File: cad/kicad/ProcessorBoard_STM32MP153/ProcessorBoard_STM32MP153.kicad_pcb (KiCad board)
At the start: 6 copper layers, 50 x 50 mm, 87 parts, among them IC301 STPMIC1BPQR, IC401 IS43LD16320A-25BLI, J201 Conn_01x03_Pin, J301 Conn_01x01_Pin, J501 SFP, U201 STM32MP153CACx, X201 ECS-3225MVQ-240-CN-TR, X501 RTL8211FS(I)-xx-xx

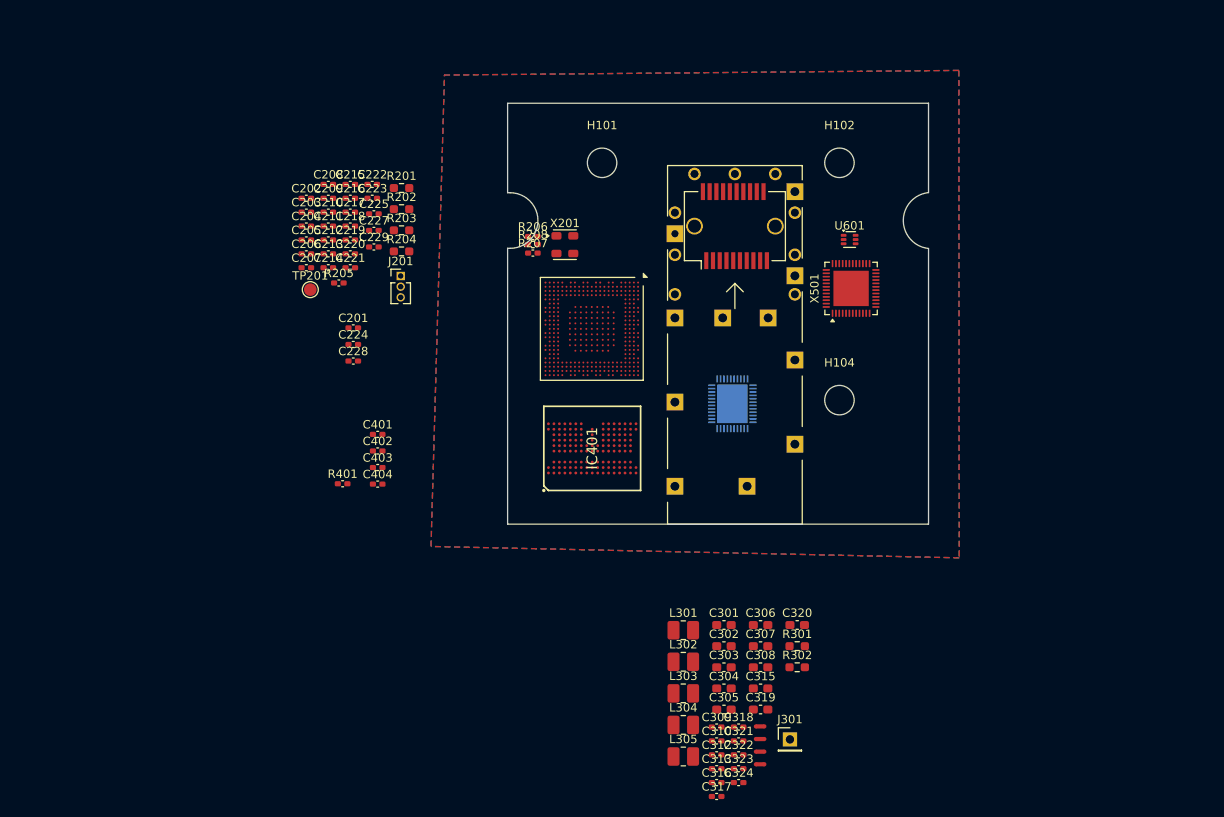
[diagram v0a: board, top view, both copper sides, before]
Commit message: new ram
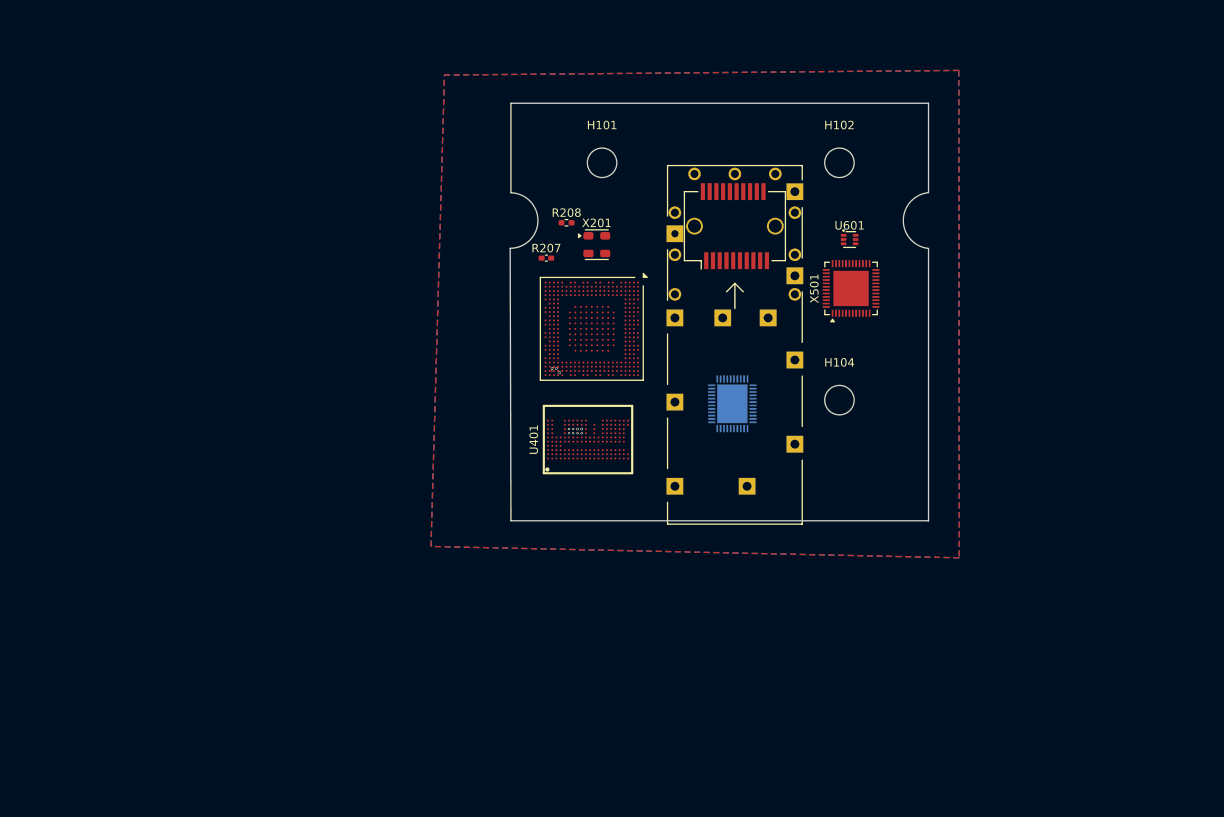
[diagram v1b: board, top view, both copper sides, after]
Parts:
- removed C201, C224, C225, C227, C228, C229, C401, C402, C403, C404: 100n, Capacitor_SMD:C_0402_1005Metric_Pad0.74x0.62mm_HandSolder
- removed C202, C203, C204, C205, C206, C207, C208, C209, C210, C211, C212, C213, C214, C215, C216, C217, C218, C221, C222, C223, C309, C312, C316, C317, C321, C324: 1u, Capacitor_SMD:C_0402_1005Metric_Pad0.74x0.62mm_HandSolder
- removed C219, C220: 1n, Capacitor_SMD:C_0402_1005Metric_Pad0.74x0.62mm_HandSolder
- removed C301, C303, C305, C307, C315, C319, C320: 10u, Capacitor_SMD:C_0603_1608Metric_Pad1.08x0.95mm_HandSolder
- removed C302, C304, C306, C308: 22u, Capacitor_SMD:C_0603_1608Metric_Pad1.08x0.95mm_HandSolder
- removed C310, C313, C318, C322, C323: 4.7u, Capacitor_SMD:C_0402_1005Metric_Pad0.74x0.62mm_HandSolder
- removed IC401: IS43LD16320A-25BLI, __WM_Local:BGA134C65P10X17_1000X1150X110
- removed J201: Conn_01x03_Pin, Connector_PinHeader_1.27mm:PinHeader_1x03_P1.27mm_Vertical
- removed J301: Conn_01x01_Pin, Connector_PinHeader_2.54mm:PinHeader_1x01_P2.54mm_Vertical
- removed L301, L302, L303, L304, L305: 1u, Inductor_SMD:L_1008_2520Metric_Pad1.43x2.20mm_HandSolder
- removed NT301, NT302, NT303, NT304: NetTie_2, NetTie:NetTie-2_SMD_Pad0.5mm
- removed R201, R202, R204: 47k, Resistor_SMD:R_0603_1608Metric_Pad0.98x0.95mm_HandSolder
- removed R203: 3090, Resistor_SMD:R_0603_1608Metric_Pad0.98x0.95mm_HandSolder
- removed R205, R401: 240, Capacitor_SMD:C_0402_1005Metric_Pad0.74x0.62mm_HandSolder
- removed R206: 10k, Capacitor_SMD:C_0402_1005Metric_Pad0.74x0.62mm_HandSolder
- removed R301, R302: 1.2k, Resistor_SMD:R_0603_1608Metric_Pad0.98x0.95mm_HandSolder
- removed TP201: TestPoint, TestPoint:TestPoint_Pad_D1.5mm
- added U401: XT61M2G8D2TA-B8BEA, __WM_Local:FBGA-162_L10.5-W8.0-P0.50_XT61M4G8D2TA, F.Cu at (139.6, 110.0)
- moved R208 4.76 mm to (137.0, 84.2)
- moved X201 3.80 mm to (140.6, 86.8)
- moved R207 1.71 mm to (134.6, 88.4)
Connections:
- J501 pad 1: Net-(J501-VeeT-Pad1) -> GND
- J501 pad 10: Net-(J501-VeeR-Pad10) -> GND
- J501 pad 11: Net-(J501-VeeR-Pad10) -> GND
- J501 pad 12: unconnected-(J501-RD--Pad12) -> /SPF/RD-
- J501 pad 13: unconnected-(J501-RD+-Pad13) -> /SPF/RD+
- J501 pad 14: Net-(J501-VeeR-Pad10) -> GND
- J501 pad 15: unconnected-(J501-VccR-Pad15) -> /SPF/3v3 3A_{max}
- J501 pad 16: unconnected-(J501-VccT-Pad16) -> /SPF/3v3 3A_{max}
- J501 pad 17: Net-(J501-VeeT-Pad1) -> GND
- J501 pad 18: unconnected-(J501-TD+-Pad18) -> /SPF/TD+
- J501 pad 19: unconnected-(J501-TD--Pad19) -> /SPF/TD-
- J501 pad 20: Net-(J501-VeeT-Pad1) -> GND
- J501 pad 4: unconnected-(J501-MOD_DEF2-Pad4) -> /SPF/MOD_SDA
- J501 pad 5: unconnected-(J501-MOD_DEF1-Pad5) -> /SPF/MOD_SCL
- J501 pad 6: unconnected-(J501-MOD_DEF0-Pad6) -> /SPF/MOD_PRZ
- J501 pad 9: Net-(J501-VeeR-Pad10) -> GND
- U601 pad 1: unconnected-(U601-GND-Pad1) -> GND
- U601 pad 2: unconnected-(U601-SW-Pad2) -> Net-(U601-SW)
- U601 pad 3: unconnected-(U601-V_{in}-Pad3) -> /Power SPF/OB_5v
- U601 pad 4: unconnected-(U601-EN-Pad4) -> /Power SPF/enable
- U601 pad 5: unconnected-(U601-FB-Pad5) -> Net-(U601-FB)
- X501 pad 1: unconnected-(X501-AV_{dd}3v3-Pad1) -> /SPF/3v3 3A_{max}
- X501 pad 12: unconnected-(X501-AV_{dd}3v3-Pad12) -> /SPF/3v3 3A_{max}
- X501 pad 22: unconnected-(X501-DV_{dd}1v0-Pad22) -> Net-(C502-Pad1)
- X501 pad 30: unconnected-(X501-AV_{dd}3v3-Pad30) -> /SPF/3v3 3A_{max}
- X501 pad 31: unconnected-(X501-V_{dd}_REG-Pad31) -> /SPF/3v3 3A_{max}
- X501 pad 32: unconnected-(X501-REG_OUT-Pad32) -> Net-(X501-REG_OUT)
- X501 pad 4: unconnected-(X501-AV_{dd}1v0-Pad4) -> Net-(C502-Pad1)
- X501 pad 45: unconnected-(X501-XTAL_IN-Pad45) -> /SPF/xtal_in
- X501 pad 46: unconnected-(X501-XTAL_OUT-Pad46) -> /SPF/xtal_out
- X501 pad 47: unconnected-(X501-DV_{dd}1v0-Pad47) -> Net-(C502-Pad1)
- X501 pad 48: unconnected-(X501-RSET-Pad48) -> /SPF/reset
- X501 pad 49: unconnected-(X501-GND-Pad49) -> GND
- X501 pad 9: unconnected-(X501-AV_{dd}1v0-Pad9) -> Net-(C502-Pad1)
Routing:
- net unconnected-(U401-DM3-PadH7): track 0.00 -> 0.95 mm, vias 0 -> 1
- net GND: track 0.00 -> 0.70 mm, vias 0 -> 1
- net /d15: track 0.00 -> 0.31 mm, vias 0 -> 2
- net unconnected-(U201-DDR_DQ25-PadY22): track 0.00 -> 0.28 mm, vias 0 -> 1
- net /d14: track 0.00 -> 0.10 mm, vias 0 -> 1
- net unconnected-(U401-DQS3-PadG8): vias 0 -> 1
- net unconnected-(U401-DQ27-PadG7): vias 0 -> 1
- net unconnected-(U401-DQ25-PadF8): vias 0 -> 1
- net /d13: vias 0 -> 1
- net /V_{dd_DDRQ}: vias 0 -> 1
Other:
- board size 50 x 50 mm -> 49.7 x 49.6 mm

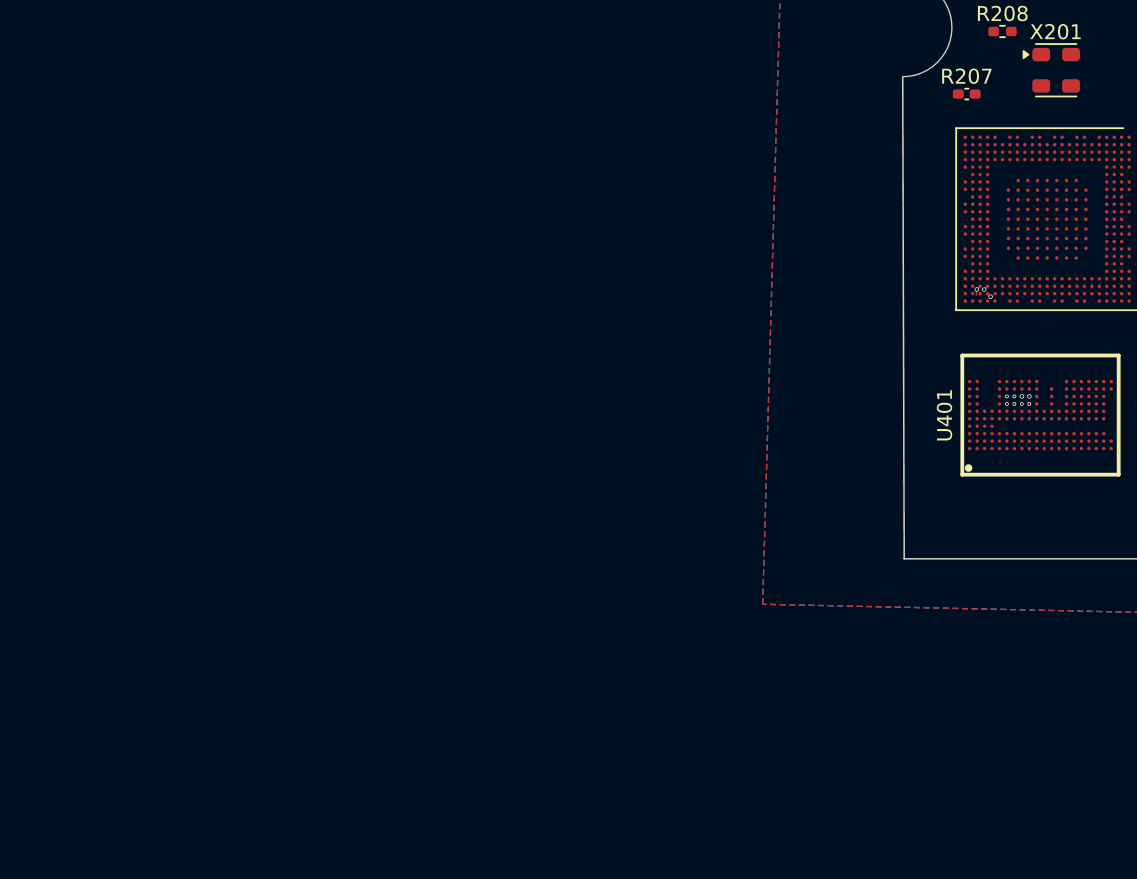
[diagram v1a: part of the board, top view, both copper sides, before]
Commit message: realtek bridge thing somewhat more wired
apparently the proper term for via skimping and what not is NFPR (non functional pad removal). all my homies love NFPR. so it is possible to route 0.5mm bga. still fighting the dog but at least cant bring it to another layer
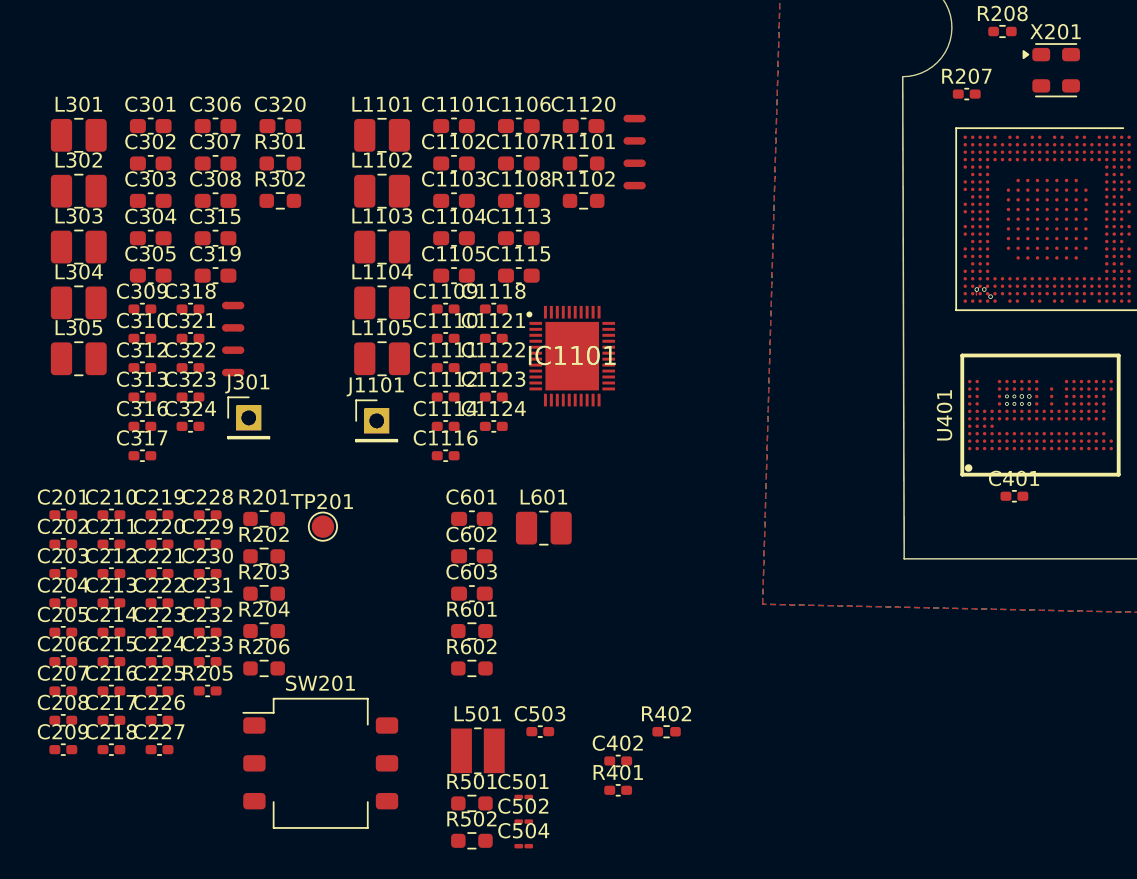
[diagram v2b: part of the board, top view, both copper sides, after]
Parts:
- added C1101: 10u, Capacitor_SMD:C_0603_1608Metric_Pad1.08x0.95mm_HandSolder, F.Cu at (100.2, 90.5)
- added C1102: 10u, Capacitor_SMD:C_0603_1608Metric_Pad1.08x0.95mm_HandSolder, F.Cu at (100.2, 93.1)
- added C1103: 10u, Capacitor_SMD:C_0603_1608Metric_Pad1.08x0.95mm_HandSolder, F.Cu at (100.2, 95.6)
- added C1104: 10u, Capacitor_SMD:C_0603_1608Metric_Pad1.08x0.95mm_HandSolder, F.Cu at (100.2, 98.1)
- added C1105: 22u, Capacitor_SMD:C_0603_1608Metric_Pad1.08x0.95mm_HandSolder, F.Cu at (100.2, 100.6)
- added C1106: 22u, Capacitor_SMD:C_0603_1608Metric_Pad1.08x0.95mm_HandSolder, F.Cu at (104.5, 90.5)
- added C1107: 22u, Capacitor_SMD:C_0603_1608Metric_Pad1.08x0.95mm_HandSolder, F.Cu at (104.5, 93.1)
- added C1108: 22u, Capacitor_SMD:C_0603_1608Metric_Pad1.08x0.95mm_HandSolder, F.Cu at (104.5, 95.6)
- added C1109: 4.7u, Capacitor_SMD:C_0402_1005Metric_Pad0.74x0.62mm_HandSolder, F.Cu at (99.6, 102.8)
- added C1110: 4.7u, Capacitor_SMD:C_0402_1005Metric_Pad0.74x0.62mm_HandSolder, F.Cu at (99.6, 104.8)
- added C1111: 1u, Capacitor_SMD:C_0402_1005Metric_Pad0.74x0.62mm_HandSolder, F.Cu at (99.6, 106.8)
- added C1112: 1u, Capacitor_SMD:C_0402_1005Metric_Pad0.74x0.62mm_HandSolder, F.Cu at (99.6, 108.7)
- added C1113: 10u, Capacitor_SMD:C_0603_1608Metric_Pad1.08x0.95mm_HandSolder, F.Cu at (104.5, 98.1)
- added C1114: 1u, Capacitor_SMD:C_0402_1005Metric_Pad0.74x0.62mm_HandSolder, F.Cu at (99.6, 110.7)
- added C1115: 10u, Capacitor_SMD:C_0603_1608Metric_Pad1.08x0.95mm_HandSolder, F.Cu at (104.5, 100.6)
- added C1116: 4.7u, Capacitor_SMD:C_0402_1005Metric_Pad0.74x0.62mm_HandSolder, F.Cu at (99.6, 112.7)
- added C1118: 4.7u, Capacitor_SMD:C_0402_1005Metric_Pad0.74x0.62mm_HandSolder, F.Cu at (102.8, 102.8)
- added C1120: 10u, Capacitor_SMD:C_0603_1608Metric_Pad1.08x0.95mm_HandSolder, F.Cu at (108.9, 90.5)
- added C1121: 1u, Capacitor_SMD:C_0402_1005Metric_Pad0.74x0.62mm_HandSolder, F.Cu at (102.8, 104.8)
- added C1122: 4.7u, Capacitor_SMD:C_0402_1005Metric_Pad0.74x0.62mm_HandSolder, F.Cu at (102.8, 106.8)
- added C1123: 1u, Capacitor_SMD:C_0402_1005Metric_Pad0.74x0.62mm_HandSolder, F.Cu at (102.8, 108.7)
- added C1124: 1u, Capacitor_SMD:C_0402_1005Metric_Pad0.74x0.62mm_HandSolder, F.Cu at (102.8, 110.7)
- added C201: 100n, Capacitor_SMD:C_0402_1005Metric_Pad0.74x0.62mm_HandSolder, F.Cu at (74.0, 116.7)
- added C202: 1u, Capacitor_SMD:C_0402_1005Metric_Pad0.74x0.62mm_HandSolder, F.Cu at (74.0, 118.6)
- added C203: 1u, Capacitor_SMD:C_0402_1005Metric_Pad0.74x0.62mm_HandSolder, F.Cu at (74.0, 120.6)
- added C204: 1u, Capacitor_SMD:C_0402_1005Metric_Pad0.74x0.62mm_HandSolder, F.Cu at (74.0, 122.6)
- added C205: 1u, Capacitor_SMD:C_0402_1005Metric_Pad0.74x0.62mm_HandSolder, F.Cu at (74.0, 124.5)
- added C206: 1u, Capacitor_SMD:C_0402_1005Metric_Pad0.74x0.62mm_HandSolder, F.Cu at (74.0, 126.5)
- added C207: 1u, Capacitor_SMD:C_0402_1005Metric_Pad0.74x0.62mm_HandSolder, F.Cu at (74.0, 128.5)
- added C208: 1u, Capacitor_SMD:C_0402_1005Metric_Pad0.74x0.62mm_HandSolder, F.Cu at (74.0, 130.4)
- added C209: 1u, Capacitor_SMD:C_0402_1005Metric_Pad0.74x0.62mm_HandSolder, F.Cu at (74.0, 132.4)
- added C210: 1u, Capacitor_SMD:C_0402_1005Metric_Pad0.74x0.62mm_HandSolder, F.Cu at (77.2, 116.7)
- added C211: 1u, Capacitor_SMD:C_0402_1005Metric_Pad0.74x0.62mm_HandSolder, F.Cu at (77.2, 118.6)
- added C212: 1u, Capacitor_SMD:C_0402_1005Metric_Pad0.74x0.62mm_HandSolder, F.Cu at (77.2, 120.6)
- added C213: 1u, Capacitor_SMD:C_0402_1005Metric_Pad0.74x0.62mm_HandSolder, F.Cu at (77.2, 122.6)
- added C214: 1u, Capacitor_SMD:C_0402_1005Metric_Pad0.74x0.62mm_HandSolder, F.Cu at (77.2, 124.5)
- added C215: 1u, Capacitor_SMD:C_0402_1005Metric_Pad0.74x0.62mm_HandSolder, F.Cu at (77.2, 126.5)
- added C216: 1u, Capacitor_SMD:C_0402_1005Metric_Pad0.74x0.62mm_HandSolder, F.Cu at (77.2, 128.5)
- added C217: 1u, Capacitor_SMD:C_0402_1005Metric_Pad0.74x0.62mm_HandSolder, F.Cu at (77.2, 130.4)
- added C218: 1u, Capacitor_SMD:C_0402_1005Metric_Pad0.74x0.62mm_HandSolder, F.Cu at (77.2, 132.4)
- added C219: 1n, Capacitor_SMD:C_0402_1005Metric_Pad0.74x0.62mm_HandSolder, F.Cu at (80.4, 116.7)
- added C220: 1n, Capacitor_SMD:C_0402_1005Metric_Pad0.74x0.62mm_HandSolder, F.Cu at (80.4, 118.6)
- added C221: 1u, Capacitor_SMD:C_0402_1005Metric_Pad0.74x0.62mm_HandSolder, F.Cu at (80.4, 120.6)
- added C222: 1u, Capacitor_SMD:C_0402_1005Metric_Pad0.74x0.62mm_HandSolder, F.Cu at (80.4, 122.6)
- added C223: 1u, Capacitor_SMD:C_0402_1005Metric_Pad0.74x0.62mm_HandSolder, F.Cu at (80.4, 124.5)
- added C224: 100n, Capacitor_SMD:C_0402_1005Metric_Pad0.74x0.62mm_HandSolder, F.Cu at (80.4, 126.5)
- added C225: 100n, Capacitor_SMD:C_0402_1005Metric_Pad0.74x0.62mm_HandSolder, F.Cu at (80.4, 128.5)
- added C226: 1u, Capacitor_SMD:C_0402_1005Metric_Pad0.74x0.62mm_HandSolder, F.Cu at (80.4, 130.4)
- added C227: 100n, Capacitor_SMD:C_0402_1005Metric_Pad0.74x0.62mm_HandSolder, F.Cu at (80.4, 132.4)
- added C228: 100n, Capacitor_SMD:C_0402_1005Metric_Pad0.74x0.62mm_HandSolder, F.Cu at (83.6, 116.7)
- added C229: 100n, Capacitor_SMD:C_0402_1005Metric_Pad0.74x0.62mm_HandSolder, F.Cu at (83.6, 118.6)
- added C230: 1u, Capacitor_SMD:C_0402_1005Metric_Pad0.74x0.62mm_HandSolder, F.Cu at (83.6, 120.6)
- added C231: 1u, Capacitor_SMD:C_0402_1005Metric_Pad0.74x0.62mm_HandSolder, F.Cu at (83.6, 122.6)
- added C232: 1u, Capacitor_SMD:C_0402_1005Metric_Pad0.74x0.62mm_HandSolder, F.Cu at (83.6, 124.5)
- added C233: 1u, Capacitor_SMD:C_0402_1005Metric_Pad0.74x0.62mm_HandSolder, F.Cu at (83.6, 126.5)
- added C301: 10u, Capacitor_SMD:C_0603_1608Metric_Pad1.08x0.95mm_HandSolder, F.Cu at (79.8, 90.5)
- added C302: 22u, Capacitor_SMD:C_0603_1608Metric_Pad1.08x0.95mm_HandSolder, F.Cu at (79.8, 93.1)
- added C303: 10u, Capacitor_SMD:C_0603_1608Metric_Pad1.08x0.95mm_HandSolder, F.Cu at (79.8, 95.6)
- added C304: 22u, Capacitor_SMD:C_0603_1608Metric_Pad1.08x0.95mm_HandSolder, F.Cu at (79.8, 98.1)
- added C305: 10u, Capacitor_SMD:C_0603_1608Metric_Pad1.08x0.95mm_HandSolder, F.Cu at (79.8, 100.6)
- added C306: 22u, Capacitor_SMD:C_0603_1608Metric_Pad1.08x0.95mm_HandSolder, F.Cu at (84.2, 90.5)
- added C307: 10u, Capacitor_SMD:C_0603_1608Metric_Pad1.08x0.95mm_HandSolder, F.Cu at (84.2, 93.1)
- added C308: 22u, Capacitor_SMD:C_0603_1608Metric_Pad1.08x0.95mm_HandSolder, F.Cu at (84.2, 95.6)
- added C309: 1u, Capacitor_SMD:C_0402_1005Metric_Pad0.74x0.62mm_HandSolder, F.Cu at (79.3, 102.8)
- added C310: 4.7u, Capacitor_SMD:C_0402_1005Metric_Pad0.74x0.62mm_HandSolder, F.Cu at (79.3, 104.8)
- added C312: 1u, Capacitor_SMD:C_0402_1005Metric_Pad0.74x0.62mm_HandSolder, F.Cu at (79.3, 106.8)
- added C313: 4.7u, Capacitor_SMD:C_0402_1005Metric_Pad0.74x0.62mm_HandSolder, F.Cu at (79.3, 108.7)
- added C315: 10u, Capacitor_SMD:C_0603_1608Metric_Pad1.08x0.95mm_HandSolder, F.Cu at (84.2, 98.1)
- added C316: 1u, Capacitor_SMD:C_0402_1005Metric_Pad0.74x0.62mm_HandSolder, F.Cu at (79.3, 110.7)
- added C317: 1u, Capacitor_SMD:C_0402_1005Metric_Pad0.74x0.62mm_HandSolder, F.Cu at (79.3, 112.7)
- added C318: 4.7u, Capacitor_SMD:C_0402_1005Metric_Pad0.74x0.62mm_HandSolder, F.Cu at (82.5, 102.8)
- added C319: 10u, Capacitor_SMD:C_0603_1608Metric_Pad1.08x0.95mm_HandSolder, F.Cu at (84.2, 100.6)
- added C320: 10u, Capacitor_SMD:C_0603_1608Metric_Pad1.08x0.95mm_HandSolder, F.Cu at (88.5, 90.5)
- added C321: 1u, Capacitor_SMD:C_0402_1005Metric_Pad0.74x0.62mm_HandSolder, F.Cu at (82.5, 104.8)
- added C322: 4.7u, Capacitor_SMD:C_0402_1005Metric_Pad0.74x0.62mm_HandSolder, F.Cu at (82.5, 106.8)
- added C323: 4.7u, Capacitor_SMD:C_0402_1005Metric_Pad0.74x0.62mm_HandSolder, F.Cu at (82.5, 108.7)
- added C324: 1u, Capacitor_SMD:C_0402_1005Metric_Pad0.74x0.62mm_HandSolder, F.Cu at (82.5, 110.7)
- added C401: 100n, Capacitor_SMD:C_0402_1005Metric_Pad0.74x0.62mm_HandSolder, F.Cu at (137.8, 115.4)
- added C402: 100n, Capacitor_SMD:C_0402_1005Metric_Pad0.74x0.62mm_HandSolder, F.Cu at (111.2, 133.2)
- added C501: 4.7u, Capacitor_SMD:C_01005_0402Metric_Pad0.57x0.30mm_HandSolder, F.Cu at (104.9, 135.6)
- added C502: 4.7u, Capacitor_SMD:C_01005_0402Metric_Pad0.57x0.30mm_HandSolder, F.Cu at (104.9, 137.2)
- added C503: 100n, Capacitor_SMD:C_0402_1005Metric_Pad0.74x0.62mm_HandSolder, F.Cu at (106.0, 131.2)
- added C504: 4.7u, Capacitor_SMD:C_01005_0402Metric_Pad0.57x0.30mm_HandSolder, F.Cu at (104.9, 138.9)
- added C601: 10u, Capacitor_SMD:C_0603_1608Metric_Pad1.08x0.95mm_HandSolder, F.Cu at (101.4, 116.9)
- added C602: 10u, Capacitor_SMD:C_0603_1608Metric_Pad1.08x0.95mm_HandSolder, F.Cu at (101.4, 119.4)
- added C603: 10u, Capacitor_SMD:C_0603_1608Metric_Pad1.08x0.95mm_HandSolder, F.Cu at (101.4, 121.9)
- added IC1101: STPMIC1BPQR, __WM_Local:QFN40P500X600X80-45N-D, F.Cu at (108.1, 106.0)
- added J1101: Conn_01x01_Pin, Connector_PinHeader_2.54mm:PinHeader_1x01_P2.54mm_Vertical, F.Cu at (95.0, 110.3)
- added J301: Conn_01x01_Pin, Connector_PinHeader_2.54mm:PinHeader_1x01_P2.54mm_Vertical, F.Cu at (86.4, 110.1)
- added L1101: 1u, Inductor_SMD:L_1008_2520Metric_Pad1.43x2.20mm_HandSolder, F.Cu at (95.3, 91.2)
- added L1102: 1u, Inductor_SMD:L_1008_2520Metric_Pad1.43x2.20mm_HandSolder, F.Cu at (95.3, 94.9)
- added L1103: 1u, Inductor_SMD:L_1008_2520Metric_Pad1.43x2.20mm_HandSolder, F.Cu at (95.3, 98.7)
- added L1104: 1u, Inductor_SMD:L_1008_2520Metric_Pad1.43x2.20mm_HandSolder, F.Cu at (95.3, 102.4)
- added L1105: 1u, Inductor_SMD:L_1008_2520Metric_Pad1.43x2.20mm_HandSolder, F.Cu at (95.3, 106.2)
- added L301: 1u, Inductor_SMD:L_1008_2520Metric_Pad1.43x2.20mm_HandSolder, F.Cu at (75.0, 91.2)
- added L302: 1u, Inductor_SMD:L_1008_2520Metric_Pad1.43x2.20mm_HandSolder, F.Cu at (75.0, 94.9)
- added L303: 1u, Inductor_SMD:L_1008_2520Metric_Pad1.43x2.20mm_HandSolder, F.Cu at (75.0, 98.7)
- added L304: 1u, Inductor_SMD:L_1008_2520Metric_Pad1.43x2.20mm_HandSolder, F.Cu at (75.0, 102.4)
- added L305: 1u, Inductor_SMD:L_1008_2520Metric_Pad1.43x2.20mm_HandSolder, F.Cu at (75.0, 106.2)
- added L501: 2.2u, Inductor_SMD:L_Ferrocore_DLG-0302, F.Cu at (101.8, 132.5)
- added L601: 1u, Inductor_SMD:L_1008_2520Metric_Pad1.43x2.20mm_HandSolder, F.Cu at (106.2, 117.5)
- added NT1101: NetTie_2, NetTie:NetTie-2_SMD_Pad0.5mm, F.Cu at (112.3, 90.0)
- added NT1102: NetTie_2, NetTie:NetTie-2_SMD_Pad0.5mm, F.Cu at (112.3, 91.5)
- added NT1103: NetTie_2, NetTie:NetTie-2_SMD_Pad0.5mm, F.Cu at (112.3, 93.0)
- added NT1104: NetTie_2, NetTie:NetTie-2_SMD_Pad0.5mm, F.Cu at (112.3, 94.5)
- added NT301: NetTie_2, NetTie:NetTie-2_SMD_Pad0.5mm, F.Cu at (85.4, 102.6)
- added NT302: NetTie_2, NetTie:NetTie-2_SMD_Pad0.5mm, F.Cu at (85.4, 104.1)
- added NT303: NetTie_2, NetTie:NetTie-2_SMD_Pad0.5mm, F.Cu at (85.4, 105.6)
- added NT304: NetTie_2, NetTie:NetTie-2_SMD_Pad0.5mm, F.Cu at (85.4, 107.1)
- added R1101: 1.2k, Resistor_SMD:R_0603_1608Metric_Pad0.98x0.95mm_HandSolder, F.Cu at (108.9, 93.1)
- added R1102: 1.2k, Resistor_SMD:R_0603_1608Metric_Pad0.98x0.95mm_HandSolder, F.Cu at (108.9, 95.6)
- added R201: 45.3k, Resistor_SMD:R_0603_1608Metric_Pad0.98x0.95mm_HandSolder, F.Cu at (87.4, 116.9)
- added R202: 45.3k, Resistor_SMD:R_0603_1608Metric_Pad0.98x0.95mm_HandSolder, F.Cu at (87.4, 119.4)
- added R203: 45.3k, Resistor_SMD:R_0603_1608Metric_Pad0.98x0.95mm_HandSolder, F.Cu at (87.4, 121.9)
- added R204: 1.2k, Resistor_SMD:R_0603_1608Metric_Pad0.98x0.95mm_HandSolder, F.Cu at (87.4, 124.5)
- added R205: 240, Capacitor_SMD:C_0402_1005Metric_Pad0.74x0.62mm_HandSolder, F.Cu at (83.6, 128.5)
- added R206: 10k, Resistor_SMD:R_0603_1608Metric_Pad0.98x0.95mm_HandSolder, F.Cu at (87.4, 127.0)
- added R301: 1.2k, Resistor_SMD:R_0603_1608Metric_Pad0.98x0.95mm_HandSolder, F.Cu at (88.5, 93.1)
- added R302: 1.2k, Resistor_SMD:R_0603_1608Metric_Pad0.98x0.95mm_HandSolder, F.Cu at (88.5, 95.6)
- added R401: 240, Capacitor_SMD:C_0402_1005Metric_Pad0.74x0.62mm_HandSolder, F.Cu at (111.2, 135.1)
- added R402: 100, Resistor_SMD:R_0402_1005Metric_Pad0.72x0.64mm_HandSolder, F.Cu at (114.5, 131.2)
- added R501: 1.2k, Resistor_SMD:R_0603_1608Metric_Pad0.98x0.95mm_HandSolder, F.Cu at (101.4, 136.0)
- added R502: 1.2k, Resistor_SMD:R_0603_1608Metric_Pad0.98x0.95mm_HandSolder, F.Cu at (101.4, 138.5)
- added R601: 45.3k, Resistor_SMD:R_0603_1608Metric_Pad0.98x0.95mm_HandSolder, F.Cu at (101.4, 124.5)
- added R602: 10k, Resistor_SMD:R_0603_1608Metric_Pad0.98x0.95mm_HandSolder, F.Cu at (101.4, 127.0)
- added SW201: SW_DIP_x03, Button_Switch_SMD:SW_DIP_SPSTx03_Slide_Omron_A6S-310x_W8.9mm_P2.54mm, F.Cu at (91.2, 133.3)
- added TP201: TestPoint, TestPoint:TestPoint_Pad_D1.5mm, F.Cu at (91.4, 117.4)
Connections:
- U201 pad A21: unconnected-(U201-DDR_DQ20-PadA21) -> /d20
- U201 pad A22: unconnected-(U201-DDR_DQ23-PadA22) -> /d23
- U201 pad AA20: unconnected-(U201-DDR_DQM3-PadAA20) -> /m3
- U201 pad AA22: unconnected-(U201-DDR_DQ31-PadAA22) -> /d31
- U201 pad AA23: unconnected-(U201-DDR_DQ30-PadAA23) -> /d30
- U201 pad AB20: unconnected-(U201-DDR_DQ27-PadAB20) -> /d27
- U201 pad AB21: unconnected-(U201-DDR_DQ26-PadAB21) -> /d26
- U201 pad AB22: unconnected-(U201-DDR_DQS3P-PadAB22) -> /s3_P
- U201 pad AB23: unconnected-(U201-DDR_DQS3N-PadAB23) -> /s3_N
- U201 pad AC21: unconnected-(U201-DDR_DQ29-PadAC21) -> /d29
- U201 pad AC22: unconnected-(U201-DDR_DQ28-PadAC22) -> /d28
- U201 pad B21: unconnected-(U201-DDR_DQ19-PadB21) -> /d19
- U201 pad B22: unconnected-(U201-DDR_DQ16-PadB22) -> /d16
- U201 pad B23: unconnected-(U201-DDR_DQS2N-PadB23) -> /s2_N
- U201 pad C22: unconnected-(U201-DDR_DQS2P-PadC22) -> /s2_P
- U201 pad C23: unconnected-(U201-DDR_DQM2-PadC23) -> /m2
- U201 pad D21: unconnected-(U201-DDR_DQ22-PadD21) -> /d22
- U201 pad D22: unconnected-(U201-DDR_DQ17-PadD22) -> /d17
- U201 pad D23: unconnected-(U201-DDR_DQ18-PadD23) -> /d18
- U201 pad E23: unconnected-(U201-DDR_DQ21-PadE23) -> /d21
- U201 pad Y22: unconnected-(U201-DDR_DQ25-PadY22) -> /d25
- U201 pad Y23: unconnected-(U201-DDR_DQ24-PadY23) -> /d24
- U401 pad A3: unconnected-(U401-WP#-PadA3) -> /WPn
- U401 pad A4: unconnected-(U401-CLE-PadA4) -> /CLE
- U401 pad A6: unconnected-(U401-IO4-PadA6) -> /flashd4
- U401 pad A7: unconnected-(U401-IO7-PadA7) -> /flashd7
- U401 pad B4: unconnected-(U401-ALE-PadB4) -> /ALE
- U401 pad B5: unconnected-(U401-RE#-PadB5) -> /REn
- U401 pad B6: unconnected-(U401-IO5-PadB6) -> /flashd5
- U401 pad C2: unconnected-(U401-IO1-PadC2) -> /flashd1
- U401 pad C3: unconnected-(U401-IO3-PadC3) -> /flashd3
- U401 pad C4: unconnected-(U401-WE#-PadC4) -> /WEn
- U401 pad C5: unconnected-(U401-R/B#-PadC5) -> /R/Bn
- U401 pad C6: unconnected-(U401-IO6-PadC6) -> /flashd6
- U401 pad D2: unconnected-(U401-IO0-PadD2) -> /flashd0
- U401 pad D3: unconnected-(U401-IO2-PadD3) -> /flashd2
- U401 pad D4: unconnected-(U401-CE#-PadD4) -> /CEn
- U401 pad E7: unconnected-(U401-DQ31-PadE7) -> /d31
- U401 pad E8: unconnected-(U401-DQ29-PadE8) -> /d29
- U401 pad E9: unconnected-(U401-DQ26-PadE9) -> /d26
- U401 pad F8: unconnected-(U401-DQ25-PadF8) -> /d25
- U401 pad G6: unconnected-(U401-DQ30-PadG6) -> /d30
- U401 pad G7: unconnected-(U401-DQ27-PadG7) -> /d27
- U401 pad G8: unconnected-(U401-DQS3-PadG8) -> /s3_P
- U401 pad G9: unconnected-(U401-DQS3#-PadG9) -> /s3_N
- U401 pad H5: unconnected-(U401-DQ28-PadH5) -> /d28
- U401 pad H6: unconnected-(U401-DQ24-PadH6) -> /d24
- U401 pad H7: unconnected-(U401-DM3-PadH7) -> /m3
- U401 pad T5: unconnected-(U401-DQ19-PadT5) -> /d19
- U401 pad T6: unconnected-(U401-DQ23-PadT6) -> /d23
- U401 pad T7: unconnected-(U401-DM2-PadT7) -> /m2
- U401 pad U6: unconnected-(U401-DQ17-PadU6) -> /d17
- U401 pad U7: unconnected-(U401-DQ20-PadU7) -> /d20
- U401 pad U8: unconnected-(U401-DQS2#-PadU8) -> /s2_N
- U401 pad U9: unconnected-(U401-DQS2-PadU9) -> /s2_P
- U401 pad V8: unconnected-(U401-DQ22-PadV8) -> /d22
- U401 pad W7: unconnected-(U401-DQ16-PadW7) -> /d16
- U401 pad W8: unconnected-(U401-DQ18-PadW8) -> /d18
- U401 pad W9: unconnected-(U401-DQ21-PadW9) -> /d21
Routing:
- net unconnected-(U401-DM3-PadH7): track 0.95 -> 0.00 mm, vias 1 -> 0
- net /m3: track 0.00 -> 0.95 mm, vias 0 -> 1
- net unconnected-(U201-DDR_DQ25-PadY22): track 0.28 -> 0.00 mm, vias 1 -> 0
- net /d25: track 0.00 -> 0.28 mm, vias 0 -> 2
- net unconnected-(U401-DQS3-PadG8): vias 1 -> 0
- net unconnected-(U401-DQ27-PadG7): vias 1 -> 0
- net unconnected-(U401-DQ25-PadF8): vias 1 -> 0
- net /s3_P: vias 0 -> 1
- net /d27: vias 0 -> 1
